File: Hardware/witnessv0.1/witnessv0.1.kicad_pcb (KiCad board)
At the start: 2 copper layers, 25 x 50 mm, 15 parts, among them J1 Conn_01x02, J2 Conn_01x02, J3 Conn_01x08, P1 USB_C_Plug_USB2.0, U1 RP2354B, U2 XL1509-3.3, U3 MC33063AD, U4 LSM6DS3, U5 ICM-20602

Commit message: esp32 mcu
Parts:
- added U6: W25Q128JVS, Package_SO:SOIC-8_5.3x5.3mm_P1.27mm, B.Cu at (115.0, 93.5)
- added Y1: F322540MUBCE2O, Crystal:Crystal_SMD_3225-4Pin_3.2x2.5mm, B.Cu at (111.9, 114.8)
- C1, C2, C3, C4, C5, C6, U2, U3, U4, U5: moved to B.Cu
- U1: value RP2354B -> ESP32-S3FN8; footprint Package_DFN_QFN:QFN-80-1EP_10x10mm_P0.4mm_EP3.4x3.4mm -> Package_DFN_QFN:QFN-56-1EP_7x7mm_P0.4mm_EP4x4mm; moved to B.Cu
- moved J3 43.0 mm to (106.8, 135.5)
- moved U2 24.8 mm to (124.0, 112.0), turned to 180 degrees
- moved C2 18.9 mm to (105.6, 105.0)
- moved C3 18.9 mm to (105.6, 109.7)
- moved C6 18.8 mm to (125.5, 106.0)
- moved C5 15.1 mm to (122.6, 105.5)
- moved U4 12.5 mm to (108.0, 100.0), turned to 180 degrees
- moved U5 12.3 mm to (121.0, 100.0), turned to 180 degrees
- moved C4 3.54 mm to (112.5, 119.5), turned to 0 degrees
- moved U3 2.50 mm to (109.0, 125.0), turned to 180 degrees
- moved C1 2.17 mm to (116.1, 100.0), turned to 180 degrees
- moved U1 1.66 mm to (113.8, 108.0), turned to 180 degrees
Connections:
- U1 pad 10: Net-(U1-DVDD-Pad10) -> unconnected-(U1-GPIO5-Pad10)
- U1 pad 15: Net-(U1-IOVDD-Pad15) -> unconnected-(U1-GPIO10-Pad15)
- U1 pad 2: unconnected-(U1-GPIO5-Pad2) -> Net-(U1-VDD3P3-Pad2)
- U1 pad 24: Net-(U1-IOVDD-Pad15) -> unconnected-(U1-GPIO18-Pad24)
- U1 pad 29: Net-(U1-IOVDD-Pad15) -> unconnected-(U1-VDD_SPI-Pad29)
- U1 pad 3: unconnected-(U1-GPIO6-Pad3) -> Net-(U1-VDD3P3-Pad2)
- U1 pad 32: Net-(U1-DVDD-Pad10) -> unconnected-(U1-SPICS0-Pad32)
- U1 pad 41: Net-(U1-IOVDD-Pad15) -> unconnected-(U1-GPIO36-Pad41)
- U1 pad 5: Net-(U1-IOVDD-Pad15) -> unconnected-(U1-GPIO0-Pad5)
- U1 pad 50: Net-(U1-IOVDD-Pad15) -> unconnected-(U1-U0RXD-Pad50)
- U1 pad 51: Net-(U1-DVDD-Pad10) -> unconnected-(U1-GPIO45-Pad51)
- U1 pad 55: unconnected-(U1-GPIO44/ADC4-Pad55) -> Net-(U1-VDDA-Pad55)
- U1 pad 56: unconnected-(U1-GPIO45/ADC5-Pad56) -> Net-(U1-VDDA-Pad55)

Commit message: power updates and some esp32 stuff
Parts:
- added BZ1: Buzzer, Buzzer_Beeper:Buzzer_Murata_PKMCS0909E, F.Cu at (122.0, 116.8)
- added C10: 10u, Capacitor_SMD:C_0805_2012Metric, B.Cu at (126.3, 129.0)
- added C11: 10u, Capacitor_SMD:C_0805_2012Metric, B.Cu at (125.2, 125.6)
- added C12: 22u, Capacitor_SMD:C_0805_2012Metric, B.Cu at (115.0, 129.9)
- added C13: 22u, Capacitor_SMD:C_0805_2012Metric, B.Cu at (117.0, 126.5)
- added C14: 22u, Capacitor_SMD:C_0805_2012Metric, B.Cu at (117.0, 129.8)
- added C15: 100n, Capacitor_SMD:C_0603_1608Metric, B.Cu at (113.2, 129.8)
- added C16: 100n, Capacitor_SMD:C_0603_1608Metric, B.Cu at (109.8, 131.2)
- added C17: 470n, Capacitor_SMD:C_0603_1608Metric, B.Cu at (109.6, 125.3)
- added C18: 10u, Capacitor_SMD:C_0805_2012Metric, B.Cu at (125.4, 116.2)
- added C19: 10u, Capacitor_SMD:C_0805_2012Metric, B.Cu at (126.2, 119.6)
- added C20: 10u, Capacitor_SMD:C_0603_1608Metric, B.Cu at (124.4, 119.7)
- added C21: 100n, Capacitor_SMD:C_0603_1608Metric, B.Cu at (120.1, 122.5)
- added C22: 10u, Capacitor_SMD:C_0603_1608Metric, B.Cu at (118.7, 120.0)
- added C23: 22u, Capacitor_SMD:C_0805_2012Metric, B.Cu at (117.5, 116.5)
- added C24: 22u, Capacitor_SMD:C_0805_2012Metric, B.Cu at (114.6, 119.9)
- added C25: 22u, Capacitor_SMD:C_0805_2012Metric, B.Cu at (116.8, 120.0)
- added C7: 100n, Capacitor_SMD:C_0603_1608Metric, B.Cu at (121.2, 132.0)
- added C8: 10u, Capacitor_SMD:C_0603_1608Metric, B.Cu at (118.8, 129.0)
- added C9: 10u, Capacitor_SMD:C_0603_1608Metric, B.Cu at (124.5, 129.0)
- added D1: LED_RGBA, Witness:0603x2 RGB, F.Cu at (108.0, 110.5)
- added L1: 1.5u, Inductor_SMD:L_1210_3225Metric, B.Cu at (121.7, 125.8)
- added L2: 2.2u, Inductor_SMD:L_1206_3216Metric, B.Cu at (109.9, 129.1)
- added L3: 1.5u, Inductor_SMD:L_1210_3225Metric, B.Cu at (121.5, 116.3)
- added R1: 100k, Resistor_SMD:R_0603_1608Metric, B.Cu at (113.2, 126.8)
- added R2: 470k, Resistor_SMD:R_0603_1608Metric, B.Cu at (114.9, 132.6)
- added R3: 150k, Resistor_SMD:R_0603_1608Metric, B.Cu at (118.0, 132.5)
- added R4: 10k, Resistor_SMD:R_0603_1608Metric, B.Cu at (124.3, 132.0)
- added R5: 4.7, Resistor_SMD:R_0603_1608Metric, B.Cu at (109.5, 127.0)
- added R6: 10k, Resistor_SMD:R_0603_1608Metric, B.Cu at (123.5, 122.3)
- added R7: 680k, Resistor_SMD:R_0603_1608Metric, B.Cu at (112.8, 120.0)
- added R8: 130k, Resistor_SMD:R_0603_1608Metric, B.Cu at (116.8, 122.8)
- added R9: 100k, Resistor_SMD:R_0603_1608Metric, B.Cu at (113.9, 122.8)
- added U7: MS5607-02BA, Package_LGA:LGA-8_3x5mm_P1.25mm, B.Cu at (111.5, 94.0)
- C6: value 100n -> 1u
- P1: footprint Connector_USB:USB_C_Receptacle_G-Switch_GT-USB-7010ASV -> KicadLibs:CONN_10164359-00011LF_AMP; moved to B.Cu
- U2: value XL1509-3.3 -> TPS63070; footprint Package_SO:SOIC-8_3.9x4.9mm_P1.27mm -> Witness:RNM0015A
- U3: value MC33063AD -> Ai-Thinker-Ra-01; footprint Package_SO:SOIC-8_3.9x4.9mm_P1.27mm -> RF_Module:Ai-Thinker-Ra-01-LoRa; moved to F.Cu
- U4: value LSM6DS3 -> LSM6DSV320XTR; footprint Package_LGA:LGA-14_3x2.5mm_P0.5mm_LayoutBorder3x4y -> Package_LGA:Bosch_LGA-14_3x2.5mm_P0.5mm
- U5: value ICM-20602 -> ICM-45686; footprint Package_LGA:LGA-16_3x3mm_P0.5mm_LayoutBorder3x5y -> Package_LGA:LGA-14_3x2.5mm_P0.5mm_LayoutBorder3x4y
- U6: value W25Q128JVS -> TPS63070; footprint Package_SO:SOIC-8_5.3x5.3mm_P1.27mm -> Witness:RNM0015A
- Y1: footprint Crystal:Crystal_SMD_3225-4Pin_3.2x2.5mm -> Oscillator:Oscillator_SMD_Abracon_ASCO-4Pin_1.6x1.2mm
- moved U6 27.1 mm to (121.5, 119.8), turned to 90 degrees
- moved U3 26.4 mm to (112.2, 98.8), turned to 0 degrees
- moved U2 17.4 mm to (121.6, 129.3), turned to 90 degrees
- moved P1 17.2 mm to (125.5, 104.9), turned to -90 degrees
- moved U4 12.6 mm to (120.0, 96.0)
- moved U5 11.1 mm to (110.0, 98.9)
- moved C5 8.21 mm to (115.0, 102.3), turned to 180 degrees
- moved C6 6.21 mm to (120.3, 109.4)
- moved C4 5.28 mm to (115.0, 114.8)
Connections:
- C3 pad 1: unconnected-(C3-Pad1) -> +3V3
- C3 pad 2: unconnected-(C3-Pad2) -> GND
- C4 pad 1: unconnected-(C4-Pad1) -> +3V3
- C4 pad 2: unconnected-(C4-Pad2) -> GND
- C5 pad 1: unconnected-(C5-Pad1) -> +3V3
- C5 pad 2: unconnected-(C5-Pad2) -> GND
- U1 pad 46: unconnected-(U1-VDD3P3_CPU-Pad46) -> +3V3
- U1 pad 55: Net-(U1-VDDA-Pad55) -> +3V3
- U1 pad 56: Net-(U1-VDDA-Pad55) -> +3V3
- U2 pad 1: unconnected-(U2-VIN-Pad1) -> Net-(U2-EN)
- U2 pad 2: unconnected-(U2-OUT-Pad2) -> Net-(U2-PG)
- U2 pad 3: unconnected-(U2-FB-Pad3) -> Net-(U2-VAUX)
- U2 pad 4: unconnected-(U2-~{EN}-Pad4) -> GND
- U2 pad 5: Net-(U2-GND-Pad5) -> Net-(U2-FB)
- U2 pad 6: Net-(U2-GND-Pad5) -> GND
- U2 pad 7: Net-(U2-GND-Pad5) -> Net-(C12-Pad1)
- U2 pad 8: Net-(U2-GND-Pad5) -> Net-(C12-Pad1)
- U3 pad 2: unconnected-(U3-SwE-Pad2) -> Net-(U3-GND-Pad16)
- U4 pad 6: Net-(U4-GND-Pad6) -> unconnected-(U4-GND-Pad6)
- U4 pad 7: Net-(U4-GND-Pad6) -> unconnected-(U4-GND-Pad7)
- U5 pad 10: Net-(U5-GND-Pad10) -> unconnected-(U5-RESV-Pad10)
- U5 pad 11: Net-(U5-GND-Pad10) -> unconnected-(U5-AP_SCLK-Pad11)
- U5 pad 12: Net-(U5-GND-Pad10) -> unconnected-(U5-AP_CS-Pad12)
- U5 pad 13: Net-(U5-GND-Pad10) -> unconnected-(U5-GND-Pad13)
- U5 pad 9: Net-(U5-GND-Pad10) -> unconnected-(U5-INT2-Pad9)
- U6 pad 1: unconnected-(U6-~{CS}-Pad1) -> Net-(U6-EN)
- U6 pad 2: unconnected-(U6-DO/IO_{1}-Pad2) -> Net-(U6-PG)
- U6 pad 3: unconnected-(U6-~{WP}/IO_{2}-Pad3) -> Net-(U6-VAUX)
- U6 pad 4: unconnected-(U6-GND-Pad4) -> GND
- U6 pad 5: unconnected-(U6-DI/IO_{0}-Pad5) -> Net-(U6-FB)
- U6 pad 6: unconnected-(U6-CLK-Pad6) -> GND
- U6 pad 7: unconnected-(U6-~{HOLD}/~{RESET}/IO_{3}-Pad7) -> +5V
- U6 pad 8: unconnected-(U6-VCC-Pad8) -> +5V

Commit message: lots of work
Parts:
- removed C1: 100n, Capacitor_SMD:C_0603_1608Metric
- removed R4: 10k, Resistor_SMD:R_0603_1608Metric
- added AE1: Antenna_Shield, Connector_Coaxial:U.FL_Molex_MCRF_73412-0110_Vertical, B.Cu at (124.3, 98.5)
- added C26: 100n, Capacitor_SMD:C_0603_1608Metric, B.Cu at (115.8, 110.6)
- added C27: 100n, Capacitor_SMD:C_0603_1608Metric, B.Cu at (108.8, 107.8)
- added C28: 100n, Capacitor_SMD:C_0603_1608Metric, B.Cu at (101.2, 81.1)
- added C29: 100n, Capacitor_SMD:C_0603_1608Metric, B.Cu at (101.2, 83.6)
- added C30: 1u, Capacitor_SMD:C_0603_1608Metric, B.Cu at (101.2, 86.1)
- added C31: 10u, Capacitor_SMD:C_0603_1608Metric, B.Cu at (101.2, 88.6)
- added C32: 100n, Capacitor_SMD:C_0603_1608Metric, B.Cu at (90.5, 123.5)
- added C33: 100n, Capacitor_SMD:C_0603_1608Metric, B.Cu at (86.5, 105.9)
- added C34: 100n, Capacitor_SMD:C_0603_1608Metric, B.Cu at (111.2, 120.4)
- added C36: 100n, Capacitor_SMD:C_0603_1608Metric, B.Cu at (78.8, 91.7)
- added C37: 100n, Capacitor_SMD:C_0603_1608Metric, B.Cu at (78.8, 94.2)
- added C38: 100n, Capacitor_SMD:C_0603_1608Metric, B.Cu at (78.8, 96.7)
- added C39: 100n, Capacitor_SMD:C_0603_1608Metric, B.Cu at (78.8, 99.2)
- added C40: 100n, Capacitor_SMD:C_0603_1608Metric, B.Cu at (78.8, 101.7)
- added C41: 100n, Capacitor_SMD:C_0603_1608Metric, B.Cu at (72.8, 91.7)
- added C42: 100n, Capacitor_SMD:C_0603_1608Metric, B.Cu at (72.8, 94.2)
- added D2: LED, LED_SMD:LED_0603_1608Metric, F.Cu at (107.6, 127.0)
- added D3: LED, LED_SMD:LED_0603_1608Metric, F.Cu at (111.5, 117.8)
- added D4: PMEG2020EH,115, Diode_SMD:D_SOD-123F, B.Cu at (124.5, 102.3)
- added J4: Conn_01x02, Jumper:SolderJumper-2_P1.3mm_Open_RoundedPad1.0x1.5mm, F.Cu at (104.6, 111.5)
- added L4: L_Small, Inductor_SMD:L_0805_2012Metric, B.Cu at (120.5, 99.2)
- added L5: L_Small, Inductor_SMD:L_0603_1608Metric, B.Cu at (86.5, 108.4)
- added Q1: SQA403EJ, Package_TO_SOT_SMD:Vishay_PowerPAK_SC70-6L_Single, B.Cu at (106.2, 124.1)
- added Q2: SQA403EJ, Package_TO_SOT_SMD:Vishay_PowerPAK_SC70-6L_Single, B.Cu at (105.7, 121.2)
- added R10: 10k, Resistor_SMD:R_0603_1608Metric, B.Cu at (126.3, 133.2)
- added R11: 35k, Resistor_SMD:R_0603_1608Metric, B.Cu at (126.3, 131.5)
- added R12: 10k, Resistor_SMD:R_0603_1608Metric, B.Cu at (124.0, 132.4)
- added R17: 1k, Resistor_SMD:R_0603_1608Metric, B.Cu at (108.0, 112.8)
- added R18: 1k, Resistor_SMD:R_0603_1608Metric, B.Cu at (108.0, 109.7)
- added R19: 1k, Resistor_SMD:R_0603_1608Metric, B.Cu at (108.0, 111.2)
- added R20: 1k, Resistor_SMD:R_0603_1608Metric, B.Cu at (106.2, 127.0)
- added R21: 1k, Resistor_SMD:R_0603_1608Metric, B.Cu at (112.3, 117.2)
- added R22: 1k, Resistor_SMD:R_0603_1608Metric, B.Cu at (86.5, 118.5)
- added R23: 4.7k, Resistor_SMD:R_0603_1608Metric, B.Cu at (86.5, 121.0)
- added R24: 4.7k, Resistor_SMD:R_0603_1608Metric, B.Cu at (86.5, 123.5)
- added R25: 4.7k, Resistor_SMD:R_0603_1608Metric, B.Cu at (82.5, 105.9)
- added R26: 4.7k, Resistor_SMD:R_0603_1608Metric, B.Cu at (82.5, 108.4)
- added R27: 4.7k, Resistor_SMD:R_0603_1608Metric, B.Cu at (82.5, 110.9)
- added R28: 4.7k, Resistor_SMD:R_0603_1608Metric, B.Cu at (82.5, 113.4)
- added R29: 4.7k, Resistor_SMD:R_0603_1608Metric, B.Cu at (82.5, 115.9)
- added R30: 0, Resistor_SMD:R_0603_1608Metric, B.Cu at (82.5, 118.5)
- added R31: 0, Resistor_SMD:R_0603_1608Metric, B.Cu at (82.5, 121.0)
- added R32: 5.1k, Resistor_SMD:R_0603_1608Metric, B.Cu at (119.7, 113.5)
- added R33: 2.5m, Resistor_SMD:R_0603_1608Metric, B.Cu at (109.3, 123.0)
- added R34: 2.5m, Resistor_SMD:R_0603_1608Metric, B.Cu at (108.9, 118.0)
- added U10: RA-01SH-P, RF_Module:Ai-Thinker-Ra-01-LoRa, F.Cu at (112.2, 100.5)
- added U8: W25N01KVZEIR, Package_SON:WSON-8-1EP_8x6mm_P1.27mm_EP3.4x4.3mm, B.Cu at (106.7, 99.5)
- added U9: USBLC6-2SC6, Package_TO_SOT_SMD:SOT-23-6, B.Cu at (115.2, 114.5)
- L1, L3: value 1.5u -> 1u
- U3: value Ai-Thinker-Ra-01 -> INA2180A3IDSG; footprint RF_Module:Ai-Thinker-Ra-01-LoRa -> Package_SON:Texas_DSG0008A_WSON-8-1EP_2x2mm_P0.5mm_EP0.9x1.6mm_ThermalVias; moved to B.Cu
- moved U3 21.9 mm to (108.8, 120.5), turned to 90 degrees
- moved C4 17.0 mm to (117.0, 98.0), turned to 90 degrees
- moved C3 14.1 mm to (113.8, 98.2)
- moved U4 13.0 mm to (107.7, 91.7)
- moved C6 11.9 mm to (108.8, 106.3), turned to 180 degrees
- moved C2 10.8 mm to (107.8, 94.4), turned to 180 degrees
- moved U5 9.76 mm to (118.2, 93.7)
- moved C5 5.51 mm to (118.5, 98.0), turned to 90 degrees
- moved J1 4.30 mm to (125.4, 93.7), turned to 90 degrees
- moved P1 4.19 mm to (125.7, 109.1)
- moved U1 3.88 mm to (115.2, 104.5)
- moved BZ1 3.34 mm to (121.2, 120.0)
- moved J2 2.04 mm to (105.5, 117.5), turned to 90 degrees
- moved U7 1.31 mm to (112.6, 93.3)
- moved C23 0.75 mm to (118.3, 116.5)
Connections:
- net Net-(P1-VBUS-PadA4) renamed VBUS
- net Net-(U7-CSB-Pad4) renamed /Sensors/MS56_CS
- BZ1 pad 1: unconnected-(BZ1-+-Pad1) -> /MCU/BUZZER
- BZ1 pad 2: unconnected-(BZ1---Pad2) -> GND
- C10 pad 1: +BATT -> /Power/BATT_POSTSW
- C11 pad 1: +BATT -> /Power/BATT_POSTSW
- C18 pad 1: +BATT -> /Power/BATT_POSTSW
- C19 pad 1: +BATT -> /Power/BATT_POSTSW
- C2 pad 1: unconnected-(C2-Pad1) -> +3V3
- C2 pad 2: unconnected-(C2-Pad2) -> GND
- C20 pad 1: +BATT -> /Power/BATT_POSTSW
- C22 pad 1: +5V -> /Power/5VSENSE+
- C23 pad 1: +5V -> /Power/5VSENSE+
- C24 pad 1: +5V -> /Power/5VSENSE+
- C25 pad 1: +5V -> /Power/5VSENSE+
- C6 pad 1: unconnected-(C6-Pad1) -> +3V3
- C6 pad 2: unconnected-(C6-Pad2) -> GND
- C9 pad 1: +BATT -> /Power/BATT_POSTSW
- D1 pad 1: unconnected-(D1-RK-Pad1) -> Net-(D1-RK)
- D1 pad 2: unconnected-(D1-GK-Pad2) -> Net-(D1-GK)
- D1 pad 3: unconnected-(D1-BK-Pad3) -> Net-(D1-BK)
- D1 pad 4: unconnected-(D1-A-Pad4) -> +3V3
- J1 pad 1: unconnected-(J1-Pin_1-Pad1) -> /MCU/RST
- J1 pad 2: unconnected-(J1-Pin_2-Pad2) -> GND
- J2 pad 1: unconnected-(J2-Pin_1-Pad1) -> +BATT
- J2 pad 2: unconnected-(J2-Pin_2-Pad2) -> GND
- P1 pad A12: Net-(P1-GND-PadA1) -> GND
- P1 pad A5: unconnected-(P1-CC-PadA5) -> Net-(P1-CC)
- P1 pad B12: Net-(P1-GND-PadA1) -> GND
- R6 pad 1: +BATT -> /Power/BATT_POSTSW
- R6 pad 2: Net-(U6-EN) -> Net-(U6-PS/SYNC)
- R7 pad 1: +5V -> /Power/5VSENSE+
- R9 pad 1: +5V -> /Power/5VSENSE+
- U1 pad 1: unconnected-(U1-LNA_IN-Pad1) -> Net-(U1-LNA_IN)
- U1 pad 20: unconnected-(U1-VDD3P3_RTC-Pad20) -> +3V3
- U1 pad 25: unconnected-(U1-GPIO19/USB_D--Pad25) -> Net-(U1-GPIO19/USB_D-)
- U1 pad 26: unconnected-(U1-GPIO20/USB_D+-Pad26) -> Net-(U1-GPIO20/USB_D+)
- U1 pad 29: unconnected-(U1-VDD_SPI-Pad29) -> +3V3
- U1 pad 30: unconnected-(U1-SPIHD-Pad30) -> /MCU/SPI_HD
- U1 pad 31: unconnected-(U1-SPIWP-Pad31) -> /MCU/SPI_WP
- U1 pad 32: unconnected-(U1-SPICS0-Pad32) -> /MCU/SPI_CS
- U1 pad 33: unconnected-(U1-SPICLK-Pad33) -> /MCU/SPI_CLK
- U1 pad 34: unconnected-(U1-SPIQ-Pad34) -> /MCU/SPI_Q
- U1 pad 35: unconnected-(U1-SPID-Pad35) -> /MCU/SPI_D
- U1 pad 4: unconnected-(U1-CHIP_PU-Pad4) -> /MCU/RST
- U1 pad 5: unconnected-(U1-GPIO0-Pad5) -> /MCU/GPIO0
- U1 pad 51: unconnected-(U1-GPIO45-Pad51) -> /MCU/GPIO45
- U1 pad 52: unconnected-(U1-GPIO46-Pad52) -> /MCU/GPIO46
- U1 pad 54: unconnected-(U1-XTAL_P-Pad54) -> /MCU/XIN
- U1 pad 57: unconnected-(U1-GND-Pad57) -> GND
- U1 pad 8: unconnected-(U1-GPIO3-Pad8) -> /MCU/GPIO3
- U2 pad 1: Net-(U2-EN) -> Net-(U2-PS/SYNC)
- U2 pad 12: +BATT -> /Power/BATT_POSTSW
- U2 pad 13: +BATT -> /Power/BATT_POSTSW
- U3 pad 1: unconnected-(U3-ANT-Pad1) -> /Power/ALL_ISENSE
- U3 pad 2: Net-(U3-GND-Pad16) -> /Power/BATT_POSTSW
- U3 pad 3: unconnected-(U3-VDD-Pad3) -> /Power/ISENSE+
- U3 pad 4: unconnected-(U3-~{RESET}-Pad4) -> GND
- U3 pad 5: unconnected-(U3-DIO0-Pad5) -> /Power/5VSENSE+
- U3 pad 6: unconnected-(U3-DIO1-Pad6) -> +5V
- U3 pad 7: unconnected-(U3-DIO2-Pad7) -> /Power/5V_ISENSE
- U3 pad 8: unconnected-(U3-DIO3-Pad8) -> +3V3
- U3 pad 9: Net-(U3-GND-Pad16) -> GND
- U4 pad 1: unconnected-(U4-SDO/SA0-Pad1) -> /Sensors/SPI1_CIPO
- U4 pad 12: unconnected-(U4-CS-Pad12) -> /Sensors/LSM_CS
- U4 pad 13: unconnected-(U4-SCL-Pad13) -> /Sensors/I2C_SCL
- U4 pad 14: unconnected-(U4-SDA-Pad14) -> /Sensors/I2C_SDA
- U4 pad 2: unconnected-(U4-SDX-Pad2) -> /Sensors/SPI1_SCLK
- U4 pad 3: unconnected-(U4-SCX-Pad3) -> /Sensors/SPI1_COPI
- U4 pad 4: unconnected-(U4-INT1-Pad4) -> /Sensors/LSM_INT1
- U4 pad 5: unconnected-(U4-VDDIO-Pad5) -> +3V3
- U4 pad 6: unconnected-(U4-GND-Pad6) -> GND
- U4 pad 7: unconnected-(U4-GND-Pad7) -> GND
- U4 pad 8: unconnected-(U4-VDD-Pad8) -> +3V3
- U4 pad 9: unconnected-(U4-INT2-Pad9) -> /Sensors/LSM_INT2
- U5 pad 1: unconnected-(U5-AP_SDO-Pad1) -> /Sensors/SPI1_CIPO
- U5 pad 11: unconnected-(U5-AP_SCLK-Pad11) -> /Sensors/SPI1_SCLK
- U5 pad 12: unconnected-(U5-AP_CS-Pad12) -> /Sensors/ICM_CS
- U5 pad 14: unconnected-(U5-AP_SDIO-Pad14) -> /Sensors/SPI1_COPI
- U5 pad 2: unconnected-(U5-MAS_DA-Pad2) -> /Sensors/I2C_SDA
- U5 pad 3: unconnected-(U5-MAS_CLK-Pad3) -> /Sensors/I2C_SCL
- U5 pad 4: unconnected-(U5-INT1-Pad4) -> /Sensors/ICM_INT1
- U5 pad 5: unconnected-(U5-VDDIO-Pad5) -> +3V3
- U5 pad 6: unconnected-(U5-GND-Pad6) -> GND
- U5 pad 8: unconnected-(U5-VDD-Pad8) -> +3V3
- U5 pad 9: unconnected-(U5-INT2-Pad9) -> /Sensors/ICM_INT2
- U6 pad 1: Net-(U6-EN) -> Net-(U6-PS/SYNC)
- U6 pad 12: +BATT -> /Power/BATT_POSTSW
- U6 pad 13: +BATT -> /Power/BATT_POSTSW
- U6 pad 14: Net-(U6-EN) -> /Power/5V_EN
- U6 pad 7: +5V -> /Power/5VSENSE+
- U6 pad 8: +5V -> /Power/5VSENSE+
- U7 pad 1: unconnected-(U7-VDD-Pad1) -> +3V3
- U7 pad 2: unconnected-(U7-PS-Pad2) -> GND
- U7 pad 3: unconnected-(U7-GND-Pad3) -> GND
- U7 pad 6: unconnected-(U7-SDO-Pad6) -> /Sensors/SPI1_CIPO
- U7 pad 7: unconnected-(U7-SDI/SDA-Pad7) -> /Sensors/SPI1_COPI
- U7 pad 8: unconnected-(U7-SCLK-Pad8) -> /Sensors/SPI1_SCLK
- Y1 pad 1: unconnected-(Y1-Tri-State-Pad1) -> +3V3
- Y1 pad 2: unconnected-(Y1-GND-Pad2) -> GND
- Y1 pad 3: unconnected-(Y1-OUT-Pad3) -> /MCU/XIN
- Y1 pad 4: unconnected-(Y1-VDD-Pad4) -> +3V3
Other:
- copper layers 2 -> 4

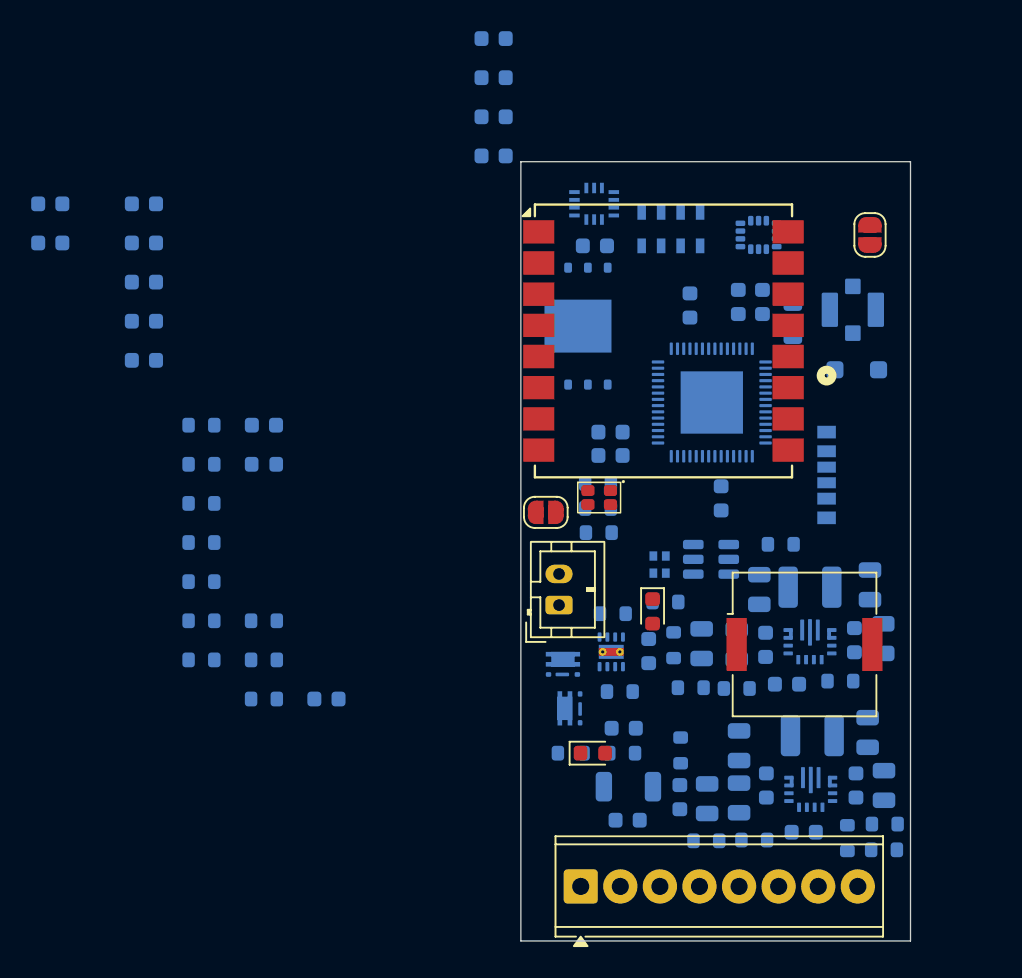
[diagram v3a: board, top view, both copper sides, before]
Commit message: micro lock conenctors and sd card soldered to baord and inital palcement done.
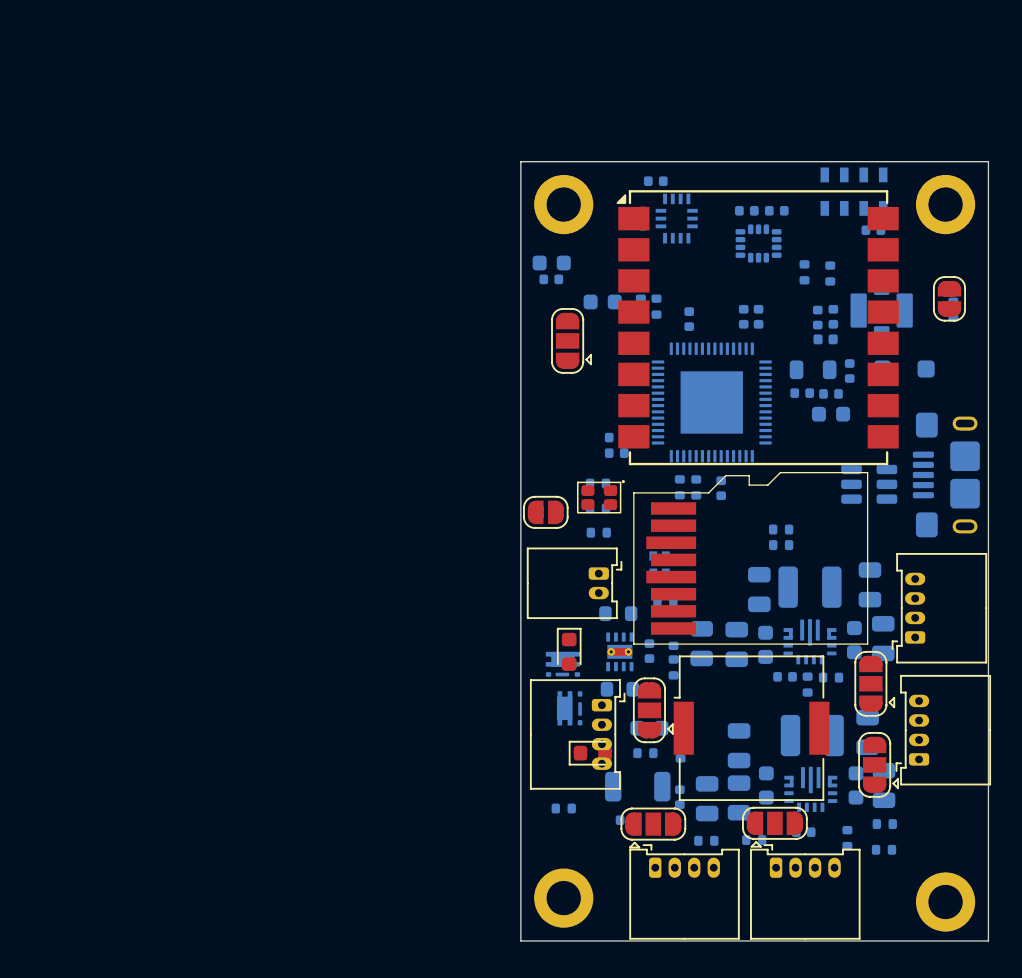
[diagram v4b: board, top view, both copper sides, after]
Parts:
- removed C2: 100n, Capacitor_SMD:C_0603_1608Metric
- removed P1: USB_C_Plug_USB2.0, KicadLibs:CONN_10164359-00011LF_AMP
- removed R32: 5.1k, Resistor_SMD:R_0603_1608Metric
- removed U8: W25N01KVZEIR, Package_SON:WSON-8-1EP_8x6mm_P1.27mm_EP3.4x4.3mm
- added C43: 10u, Capacitor_SMD:C_0603_1608Metric, B.Cu at (108.2, 98.0)
- added H4: MountingHole_Pad, MountingHole:MountingHole_2.2mm_M2_DIN965_Pad, F.Cu at (105.8, 136.2)
- added H5: MountingHole_Pad, MountingHole:MountingHole_2.2mm_M2_DIN965_Pad, F.Cu at (130.2, 136.5)
- added H6: MountingHole_Pad, MountingHole:MountingHole_2.2mm_M2_DIN965_Pad, F.Cu at (105.8, 91.8)
- added H7: MountingHole_Pad, MountingHole:MountingHole_2.2mm_M2_DIN965_Pad, F.Cu at (130.2, 91.8)
- added J10: Micro_SD_Card, microSD_Card:microSD_Card, F.Cu at (117.8, 115.0)
- added J5: Conn_01x04, Witness:Molex_MicroLock-2200980471-01x04-Horizontal, F.Cu at (111.6, 134.3)
- added J6: Conn_01x04, Witness:Molex_MicroLock-2200980471-01x04-Horizontal, F.Cu at (119.4, 134.3)
- added J7: Conn_01x04, Witness:Molex_MicroLock-2200980471-01x04-Horizontal, F.Cu at (108.2, 123.9)
- added J8: Conn_01x04, Witness:Molex_MicroLock-2200980471-01x04-Horizontal, F.Cu at (128.6, 127.3)
- added J9: Conn_01x04, Witness:Molex_MicroLock-2200980471-01x04-Horizontal, F.Cu at (128.3, 119.5)
- added JP1: SolderJumper_3_Open, Jumper:SolderJumper-3_P1.3mm_Open_RoundedPad1.0x1.5mm, F.Cu at (111.5, 131.5)
- added JP2: SolderJumper_3_Open, Jumper:SolderJumper-3_P1.3mm_Open_RoundedPad1.0x1.5mm, F.Cu at (119.3, 131.4)
- added JP3: SolderJumper_3_Open, Jumper:SolderJumper-3_P1.3mm_Open_RoundedPad1.0x1.5mm, F.Cu at (111.2, 124.2)
- added JP4: SolderJumper_3_Open, Jumper:SolderJumper-3_P1.3mm_Open_RoundedPad1.0x1.5mm, F.Cu at (125.7, 127.7)
- added JP5: SolderJumper_3_Open, Jumper:SolderJumper-3_P1.3mm_Open_RoundedPad1.0x1.5mm, F.Cu at (125.5, 122.5)
- added JP6: SolderJumper_3_Open, Jumper:SolderJumper-3_P1.3mm_Open_RoundedPad1.0x1.5mm, F.Cu at (106.0, 100.5)
- C15, C16, C21, C26, C27, C28, C29, C3, C30, C32, C33, C34, C36, C37, C38, C39, C4, C40, C42, C5, C6, C7: footprint Capacitor_SMD:C_0603_1608Metric -> Capacitor_SMD:C_0402_1005Metric
- C41: value 100n -> 10u
- J2: footprint Connector_JST:JST_PH_B2B-PH-K_1x02_P2.00mm_Vertical -> Witness:Molex_Micro_Lock_2200980271_01x02_Horizontal
- J3: value Conn_01x08 -> USB_B_Micro; footprint TerminalBlock_Phoenix:TerminalBlock_Phoenix_MPT-0,5-8-2.54_1x08_P2.54mm_Horizontal -> Connector_USB:USB_Micro-B_Amphenol_10118193-0002LF_Horizontal; moved to B.Cu
- L4: value L_Small -> 10n
- L5: footprint Inductor_SMD:L_0603_1608Metric -> Inductor_SMD:L_0402_1005Metric
- R1, R10, R11, R12, R17, R18, R19, R2, R20, R21, R22, R23, R24, R25, R26, R27, R28, R29, R3, R30, R31, R5, R6, R7, R8, R9: footprint Resistor_SMD:R_0603_1608Metric -> Resistor_SMD:R_0402_1005Metric
- moved R22 48.5 mm to (130.8, 98.5), turned to 90 degrees
- moved C38 46.9 mm to (125.6, 93.4)
- moved R24 44.2 mm to (121.2, 96.1), turned to 90 degrees
- moved R25 41.5 mm to (122.8, 96.2), turned to -90 degrees
- moved C39 41.2 mm to (119.4, 92.2)
- moved C32 39.9 mm to (122.0, 99.0), turned to 90 degrees
- moved C40 39.9 mm to (117.5, 92.2), turned to 0 degrees
- moved R29 37.3 mm to (119.7, 113.6)
- moved R28 37.2 mm to (119.7, 112.6), turned to 0 degrees
- moved C33 37.2 mm to (123.0, 99.0), turned to 90 degrees
- moved L5 36.9 mm to (122.5, 100.4), turned to 0 degrees
- moved J3 36.1 mm to (131.5, 109.1), turned to -90 degrees
- moved R30 32.9 mm to (114.2, 109.9), turned to 90 degrees
- moved C36 32.9 mm to (111.7, 90.2)
- moved R31 32.6 mm to (113.2, 109.9), turned to 90 degrees
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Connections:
- J3 pad 1: unconnected-(J3-Pin_1-Pad1) -> VBUS
- J3 pad 2: unconnected-(J3-Pin_2-Pad2) -> Net-(J3-D-)
- J3 pad 3: unconnected-(J3-Pin_3-Pad3) -> Net-(J3-D+)
- J3 pad 5: unconnected-(J3-Pin_5-Pad5) -> GND
- R30 pad 1: /MCU/USB_D+ -> /MCU/USB_D-
- U1 pad 30: /MCU/SPI_HD -> unconnected-(U1-SPIHD-Pad30)
- U1 pad 31: /MCU/SPI_WP -> unconnected-(U1-SPIWP-Pad31)
- U1 pad 32: /MCU/SPI_CS -> unconnected-(U1-SPICS0-Pad32)
- U1 pad 33: /MCU/SPI_CLK -> unconnected-(U1-SPICLK-Pad33)
- U1 pad 34: /MCU/SPI_Q -> unconnected-(U1-SPIQ-Pad34)
- U1 pad 35: /MCU/SPI_D -> unconnected-(U1-SPID-Pad35)
- U10 pad 5: +3V3 -> Net-(JP6-C)
- U9 pad 1: Net-(P1-D-) -> /IO/USB_D+
- U9 pad 3: Net-(P1-D+) -> /IO/USB_D+
- U9 pad 4: /IO/USB_D+ -> Net-(J3-D-)
- U9 pad 6: /IO/USB_D+ -> Net-(J3-D+)
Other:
- board size 25 x 50 mm -> 30 x 50 mm
